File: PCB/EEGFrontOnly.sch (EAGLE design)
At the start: 103 parts, among them IC1 ADS1299-X, IC2 ADUM3151-3, U1 LP2985-33DBVT, U10 ISO721D, U2 B0505S-1WB0505S-1W, U3 TPS60403DBVT, U4 TPS73225DBVR, U5 TPS73225DBVR, U6 TPD4E1B06DCKR, U7 TPD4E1B06DCKR, U8 TPD4E1B06DCKR, U9 HT7333

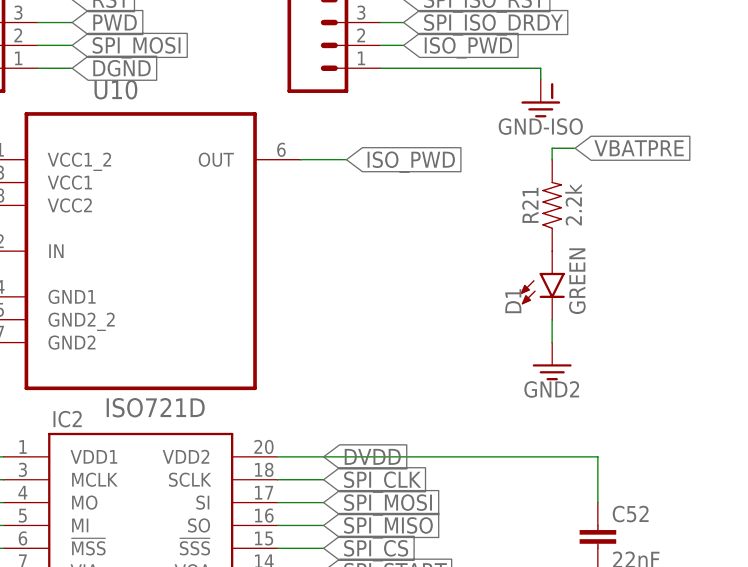
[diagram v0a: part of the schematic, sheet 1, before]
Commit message: update EEG ADS PCB
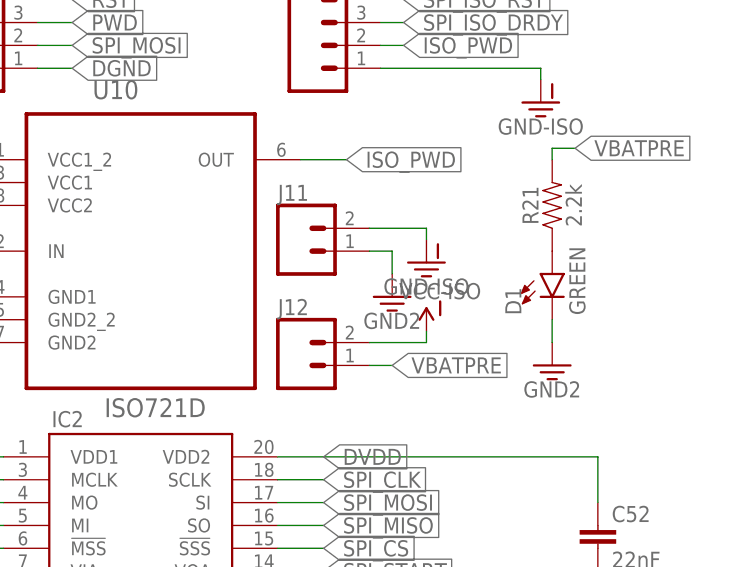
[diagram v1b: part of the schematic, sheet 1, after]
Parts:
- removed C48: 4.7nF, SparkFun-Capacitors:4.7NF-0402
- added J11, J12: (no value), SparkFun-Connectors:CONN_02
- C39: value 4.7nF -> NI
- R4: value 4.99K -> 0OHM; device SparkFun-Resistors:4.99KOHM-0402 -> SparkFun-Resistors:0OHM
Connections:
- net AGND: no longer C39.2, C40.2, C41.2, C42.2, C43.2, C44.2, C45.2, C46.2, C47.2, C48.2
- net GND: now also J11.1
- net GND-ISO: now also J11.2
- net N$12: now also C39.2, C40.2, C41.2, C42.2, C43.2, C44.2, C45.2, C46.2, C47.2; no longer C48.1
- net VBATPRE: now also J12.1
- net VCC-ISO: now also J12.2
